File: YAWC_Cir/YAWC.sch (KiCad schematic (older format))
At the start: 5 parts, among them P1 JST-PH_2, U1 TPS769XX

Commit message: Stuff
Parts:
- added R2, R3: 4k7, symbol R
- added U3: MMA845Q, symbol MMA845Q
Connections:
- net GND: now also U3.10 (GND), U3.12 (GND), U3.5 (GND), U3.7 (SAO)
- net VCC: now also R2.1, R3.1, U3.1 (VCC), U3.14 (VCC)
- new net SCL: R3.2, U3.4 (SCL)
- new net SDA: R2.2, U3.6 (SDA)
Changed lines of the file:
@@
 LIBS:opto
 LIBS:atmel
+LIBS:MySymbols
+LIBS:MyComponents
 LIBS:contrib
 LIBS:valves
@@
 Text GLabel 4350 1150 1    60   Input ~ 0
 Bth
+$Comp
+L MMA845Q U3
+U 1 1 539AF65E
+P 6250 2650
+F 0 "U3" H 6100 3300 60  0000 C CNN
+F 1 "MMA845Q" H 6350 2250 60  0000 C CNN
+F 2 "" H 6250 2650 60  0000 C CNN
+F 3 "" H 6250 2650 60  0000 C CNN
+	1    6250 2650
+	1    0    0    -1
+$EndComp
+Text Label 5750 2150 2    60   ~ 0
+VCC
+Text Label 5750 2550 2    60   ~ 0
+GND
+Text Label 7150 2550 0    60   ~ 0
+GND
+Wire Wire Line
+	6850 2550 7150 2550
+Wire Wire Line
+	6850 2750 7150 2750
+Wire Wire Line
+	7150 2750 7150 2550
+$Comp
+L R R3
+U 1 1 539AF7E0
+P 5200 2150
+F 0 "R3" V 5280 2150 40  0000 C CNN
+F 1 "4k7" V 5207 2151 40  0000 C CNN
+F 2 "" V 5130 2150 30  0000 C CNN
+F 3 "" H 5200 2150 30  0000 C CNN
+	1    5200 2150
+	1    0    0    -1
+$EndComp
+$Comp
+L R R2
+U 1 1 539AF849
+P 4800 2150
+F 0 "R2" V 4880 2150 40  0000 C CNN
+F 1 "4k7" V 4807 2151 40  0000 C CNN
+F 2 "" V 4730 2150 30  0000 C CNN
+F 3 "" H 4800 2150 30  0000 C CNN
+	1    4800 2150
+	1    0    0    -1
+$EndComp
+Wire Wire Line
+	4800 1900 6850 1900
+Wire Wire Line
+	5750 1900 5750 2150
+Connection ~ 5200 1900
+Wire Wire Line
+	5200 2400 5200 2450
+Wire Wire Line
+	5200 2450 5750 2450
+Wire Wire Line
+	4800 2650 5750 2650
+Wire Wire Line
+	5750 2750 5650 2750
+Wire Wire Line
+	5650 2750 5650 2550
+Wire Wire Line
+	5650 2550 5750 2550
+Wire Wire Line
+	6850 1900 6850 2350
+Connection ~ 5750 1900
+Text GLabel 4800 2650 0    60   Input ~ 0
+SDA
+Text GLabel 5200 2450 0    60   Input ~ 0
+SCL
+Wire Wire Line
+	4800 2400 4800 2650
+Connection ~ 4950 2650
 $EndSCHEMATC

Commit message: More updates. Foot prints still to check
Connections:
- no-connect marks 0 -> 9
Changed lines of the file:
@@
 	2200 1950 2200 2200
-Wire Wire Line
-	1800 2000 3900 2000
 Wire Wire Line
 	1800 2000 1800 1750
@@
 	1    0    0    -1
 $EndComp
-Wire Wire Line
-	3900 2000 3900 1950
-Connection ~ 3200 2000
-Wire Wire Line
-	2750 1700 2750 2000
-Connection ~ 2750 2000
 $Comp
 L CONN_4 Amp1
@@
 F1 "Micro.sch" 60
 $EndSheet
-$Comp
-L GND #PWR02
-U 1 1 5398AB48
-P 2000 3300
-F 0 "#PWR02" H 2000 3300 30  0001 C CNN
-F 1 "GND" H 2000 3230 30  0001 C CNN
-F 2 "" H 2000 3300 60  0000 C CNN
-F 3 "" H 2000 3300 60  0000 C CNN
-	1    2000 3300
-	1    0    0    -1
-$EndComp
-Wire Wire Line
-	1800 3150 2000 3150
-Wire Wire Line
-	2000 3150 2000 3300
 Text GLabel 3600 1150 1    60   Input ~ 0
 GND
@@
 	4800 2400 4800 2650
 Connection ~ 4950 2650
+NoConn ~ 6850 2450
+NoConn ~ 6850 2650
+NoConn ~ 6850 2850
+NoConn ~ 3650 1700
+NoConn ~ 5750 2350
+NoConn ~ 6850 2250
+NoConn ~ 6850 2150
+NoConn ~ 5750 2850
+NoConn ~ 5750 2250
+Wire Wire Line
+	1800 3150 2000 3150
+Wire Wire Line
+	3200 2000 3200 2350
+Wire Wire Line
+	1800 2000 2200 2000
+Text Label 2000 3150 0    60   ~ 0
+GND
+$Comp
+L GND #PWR02
+U 1 1 539EE6EA
+P 2000 3250
+F 0 "#PWR02" H 2000 3250 30  0001 C CNN
+F 1 "GND" H 2000 3180 30  0001 C CNN
+F 2 "" H 2000 3250 60  0000 C CNN
+F 3 "" H 2000 3250 60  0000 C CNN
+	1    2000 3250
+	1    0    0    -1
+$EndComp
+Wire Wire Line
+	2000 3150 2000 3250
+$Comp
+L GND #PWR03
+U 1 1 539EF1A8
+P 3200 2350
+F 0 "#PWR03" H 3200 2350 30  0001 C CNN
+F 1 "GND" H 3200 2280 30  0001 C CNN
+F 2 "" H 3200 2350 60  0000 C CNN
+F 3 "" H 3200 2350 60  0000 C CNN
+	1    3200 2350
+	1    0    0    -1
+$EndComp
+Wire Wire Line
+	2750 1700 2750 2000
+Wire Wire Line
+	2750 2000 3900 2000
+Wire Wire Line
+	3900 2000 3900 1950
+Connection ~ 3200 2000
 $EndSCHEMATC

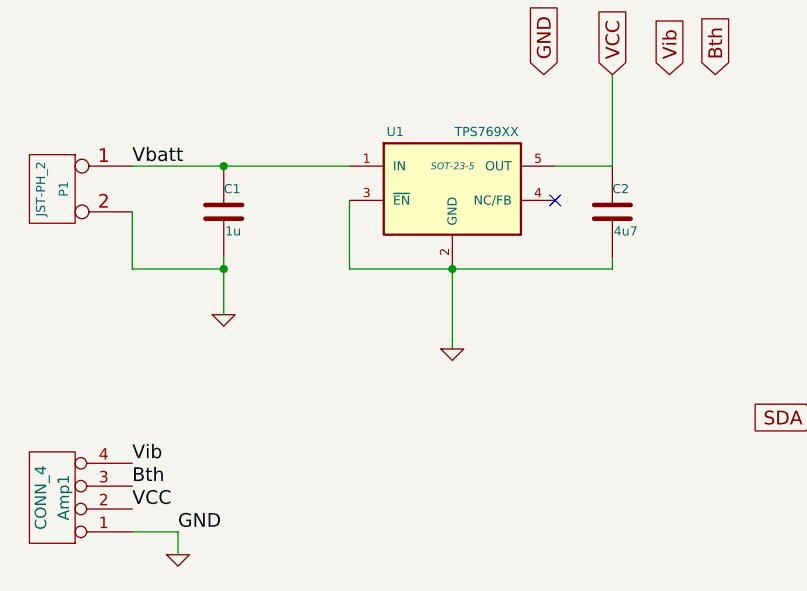
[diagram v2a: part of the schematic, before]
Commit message: Route not finished. Components done
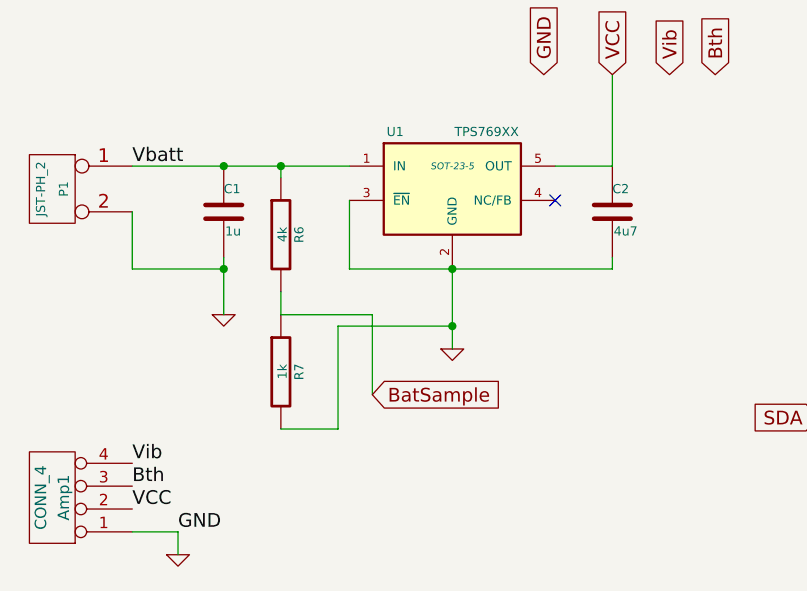
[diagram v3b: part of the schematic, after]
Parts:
- added R6: 4k, symbol R
- added R7: 1k, symbol R
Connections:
- net GND: now also R7.2
- net Vbatt: now also R6.1
- new net BatSample: R6.2, R7.1
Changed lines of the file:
@@
 	1    0    0    -1
 $EndComp
-Wire Wire Line
-	1800 1550 2750 1550
 Connection ~ 2200 1550
 Wire Wire Line
@@
 	3900 2000 3900 1950
 Connection ~ 3200 2000
+Wire Wire Line
+	1800 1550 2750 1550
+$Comp
+L R R6
+U 1 1 53A1C4D0
+P 2450 1850
+F 0 "R6" V 2530 1850 40  0000 C CNN
+F 1 "4k" V 2457 1851 40  0000 C CNN
+F 2 "" V 2380 1850 30  0000 C CNN
+F 3 "" H 2450 1850 30  0000 C CNN
+	1    2450 1850
+	1    0    0    -1
+$EndComp
+$Comp
+L R R7
+U 1 1 53A1C505
+P 2450 2450
+F 0 "R7" V 2530 2450 40  0000 C CNN
+F 1 "1k" V 2457 2451 40  0000 C CNN
+F 2 "" V 2380 2450 30  0000 C CNN
+F 3 "" H 2450 2450 30  0000 C CNN
+	1    2450 2450
+	1    0    0    -1
+$EndComp
+Wire Wire Line
+	2450 1600 2450 1550
+Connection ~ 2450 1550
+Wire Wire Line
+	2450 2200 2450 2100
+Wire Wire Line
+	2450 2700 2700 2700
+Wire Wire Line
+	2700 2700 2700 2250
+Wire Wire Line
+	2700 2250 3200 2250
+Connection ~ 3200 2250
+Wire Wire Line
+	2450 2200 2850 2200
+Text GLabel 2850 2550 2    60   Input ~ 0
+BatSample
+Wire Wire Line
+	2850 2200 2850 2550
 $EndSCHEMATC

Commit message: Add Keys project
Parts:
- C1, C2: symbol C -> C-RESCUE-YAWC
- R2, R3, R6, R7: symbol R -> R-RESCUE-YAWC
- U1: symbol TPS769XX -> TPS769XX-RESCUE-YAWC
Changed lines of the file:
@@
 EESchema Schematic File Version 2
+LIBS:YAWC-rescue
 LIBS:power
 LIBS:device
@@
 LIBS:memory
 LIBS:xilinx
-LIBS:special
 LIBS:microcontrollers
 LIBS:dsp
@@
 LIBS:valves
 LIBS:YAWC-cache
-EELAYER 24 0
+EELAYER 25 0
 EELAYER END
 $Descr A4 11693 8268
@@
 $EndComp
 $Comp
-L TPS769XX U1
+L TPS769XX-RESCUE-YAWC U1
 U 1 1 538F6803
 P 3200 1700
@@
 $EndComp
 $Comp
-L C C1
+L C-RESCUE-YAWC C1
 U 1 1 538F685C
 P 2200 1750
@@
 	3900 1550 3650 1550
 $Comp
-L GND #PWR01
+L GND-RESCUE-YAWC #PWR01
 U 1 1 538F68DF
 P 2200 2200
@@
 $EndComp
 $Comp
-L C C2
+L C-RESCUE-YAWC C2
 U 1 1 538F6921
 P 3900 1750
@@
 	7150 2750 7150 2550
 $Comp
-L R R3
+L R-RESCUE-YAWC R3
 U 1 1 539AF7E0
 P 5200 2150
@@
 $EndComp
 $Comp
-L R R2
+L R-RESCUE-YAWC R2
 U 1 1 539AF849
 P 4800 2150
@@
 GND
 $Comp
-L GND #PWR02
+L GND-RESCUE-YAWC #PWR02
 U 1 1 539EE6EA
 P 2000 3250
@@
 	2000 3150 2000 3250
 $Comp
-L GND #PWR03
+L GND-RESCUE-YAWC #PWR03
 U 1 1 539EF1A8
 P 3200 2350
@@
 	1800 1550 2750 1550
 $Comp
-L R R6
+L R-RESCUE-YAWC R6
 U 1 1 53A1C4D0
 P 2450 1850
@@
 $EndComp
 $Comp
-L R R7
+L R-RESCUE-YAWC R7
 U 1 1 53A1C505
 P 2450 2450
